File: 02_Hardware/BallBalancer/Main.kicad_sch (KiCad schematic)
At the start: 59 parts, among them J1 USB_B_Micro, J2 Raspberry PI UART, J3 SWD, J4 Reference switch 1, J5 ENCODER 1, J6 ENCODER 2, J7 Reference switch 2, U1 STM32L412K8Tx, U2 USBLC6-2SC6

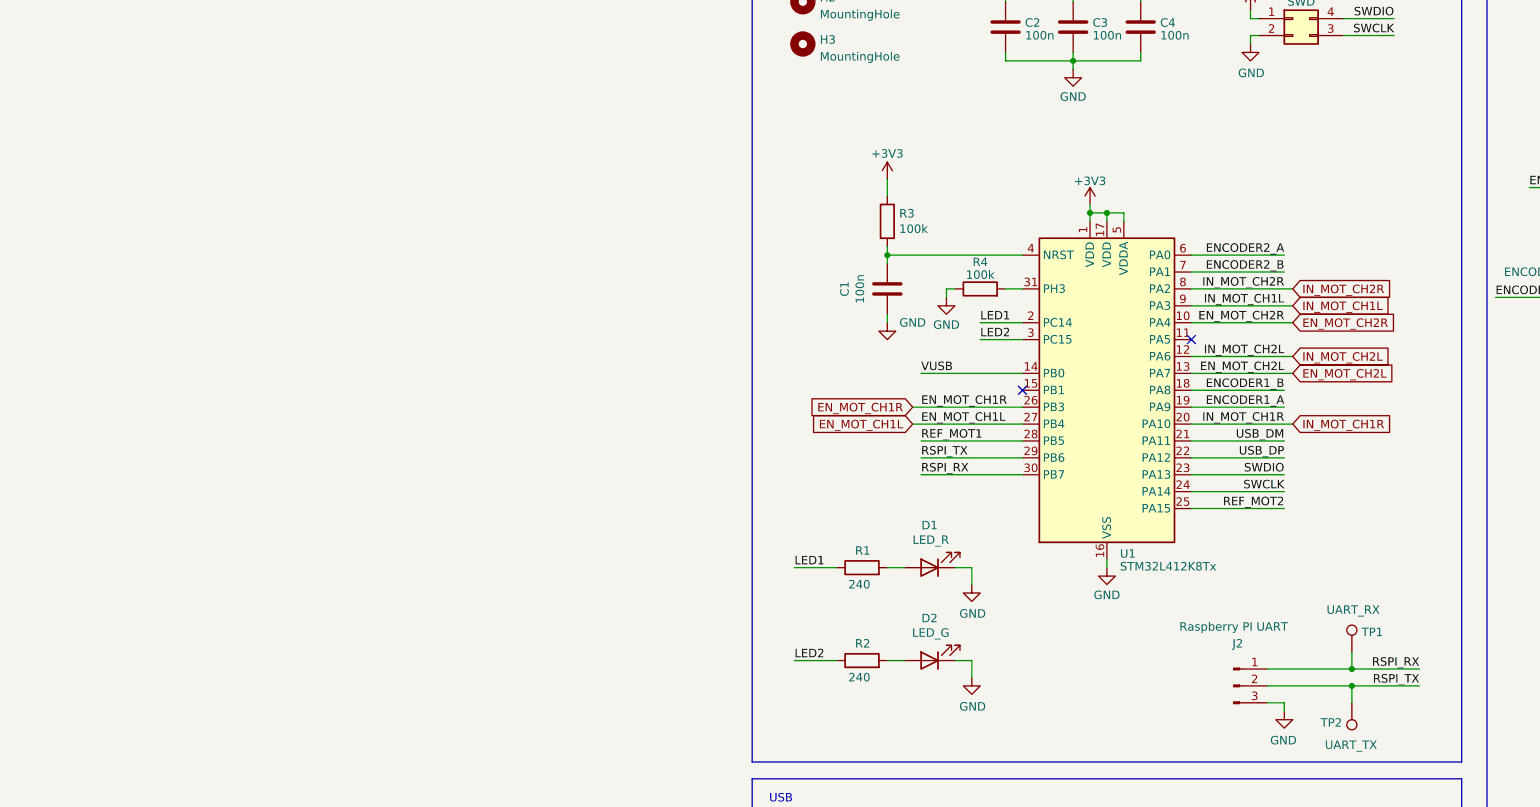
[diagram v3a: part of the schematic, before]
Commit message: replace microcontroller
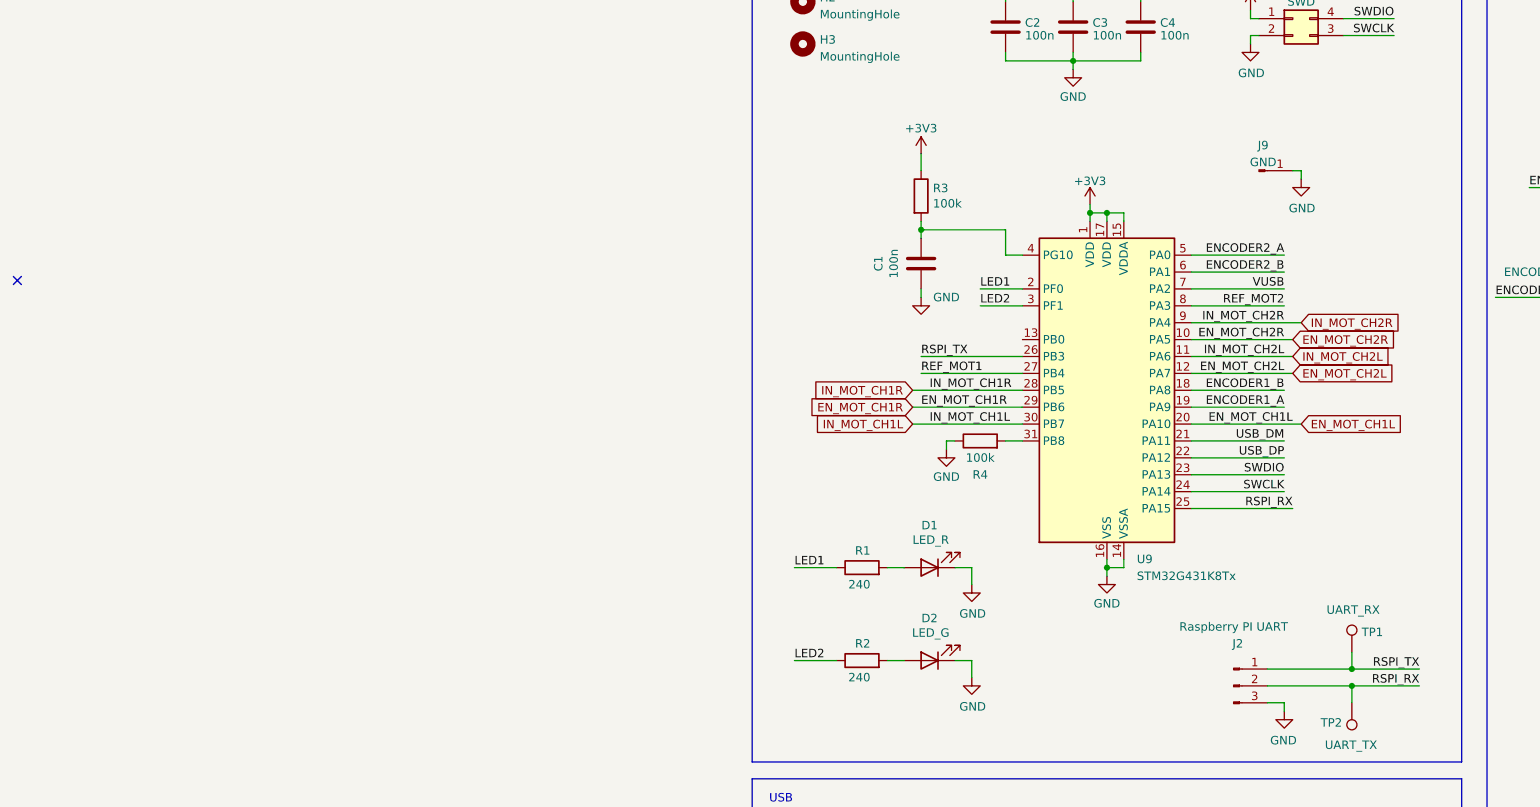
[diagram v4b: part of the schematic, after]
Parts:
- removed U1: STM32L412K8Tx, Package_QFP:LQFP-32_7x7mm_P0.8mm, symbol MCU_ST_STM32L4:STM32L412K8Tx
- added J9: GND, Connector_PinHeader_2.54mm:PinHeader_1x01_P2.54mm_Vertical, symbol Connector:Conn_01x01_Pin
- added U9: STM32G431K8Tx, Package_QFP:LQFP-32_7x7mm_P0.8mm, symbol MCU_ST_STM32G4:STM32G431K8Tx
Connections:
- net +3V3: now also U9.1 (VDD), U9.15 (VDDA), U9.17 (VDD)
- net ENCODER1_A: now also U9.19 (PA9)
- net ENCODER1_B: now also U9.18 (PA8)
- net ENCODER2_A: now also U9.5 (PA0)
- net ENCODER2_B: now also U9.6 (PA1)
- net EN_MOT_CH1L: now also U9.20 (PA10)
- net EN_MOT_CH1R: now also U9.29 (PB6)
- net EN_MOT_CH2L: now also U9.12 (PA7)
- net EN_MOT_CH2R: now also U9.10 (PA5)
- net GND: now also J9.1 (Pin_1), U9.14 (VSSA), U9.16 (VSS), U9.32 (VSS)
- net IN_MOT_CH1L: now also U9.30 (PB7)
- net IN_MOT_CH1R: now also U9.28 (PB5)
- net IN_MOT_CH2L: now also U9.11 (PA6)
- net IN_MOT_CH2R: now also U9.9 (PA4)
- net LED1: now also U9.2 (PF0)
- net LED2: now also U9.3 (PF1)
- net REF_MOT1: now also U9.27 (PB4)
- net REF_MOT2: now also U9.8 (PA3)
- net RSPI_RX: now also J2.2 (Pin_2), TP2.1, U9.25 (PA15); no longer J2.1 (Pin_1), TP1.1
- net RSPI_TX: now also J2.1 (Pin_1), TP1.1, U9.26 (PB3); no longer J2.2 (Pin_2), TP2.1
- net SWCLK: now also U9.24 (PA14)
- net SWDIO: now also U9.23 (PA13)
- net USB_DM: now also U9.21 (PA11)
- net USB_DP: now also U9.22 (PA12)
- net VUSB: now also U9.7 (PA2)
- net at R4.2: now also U9.31 (PB8)
- net at C1.2, R3.2: now also U9.4 (PG10)
- no-connect marks 5 -> 4
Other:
- moved on the sheet: C1, R3, R4

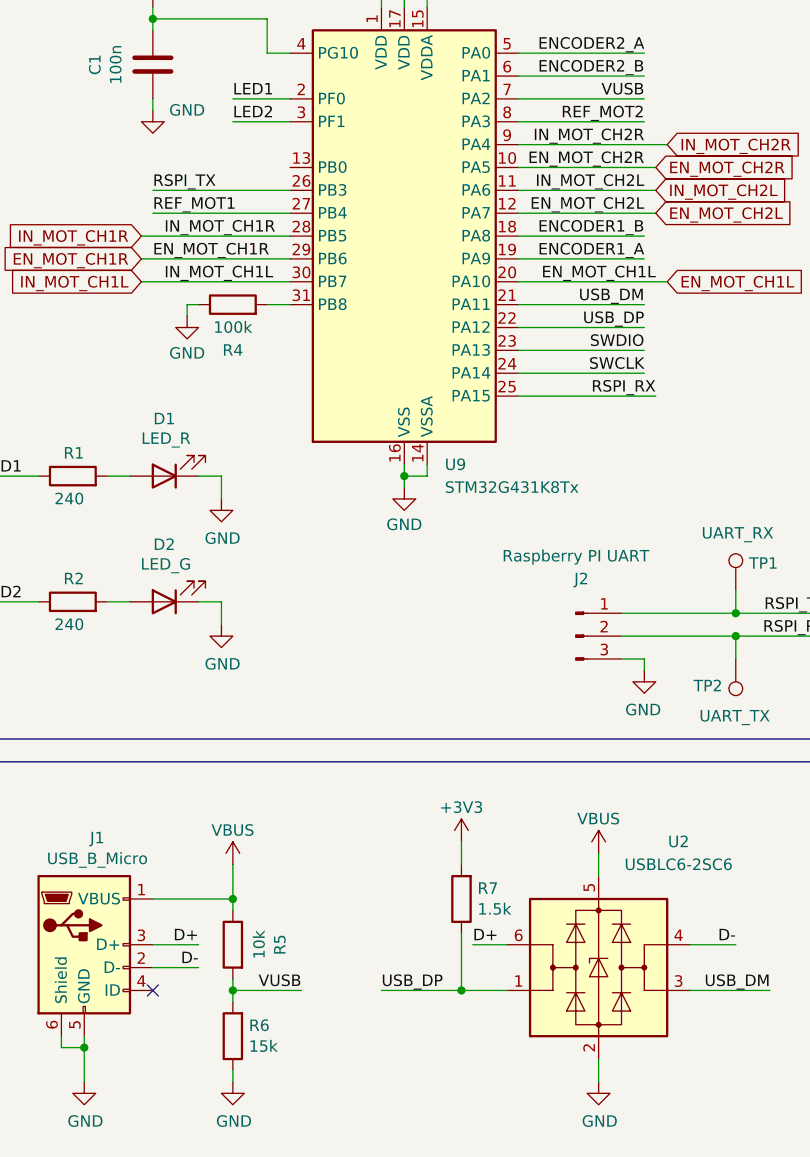
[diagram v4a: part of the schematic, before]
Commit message: Layout completed with stm32g431
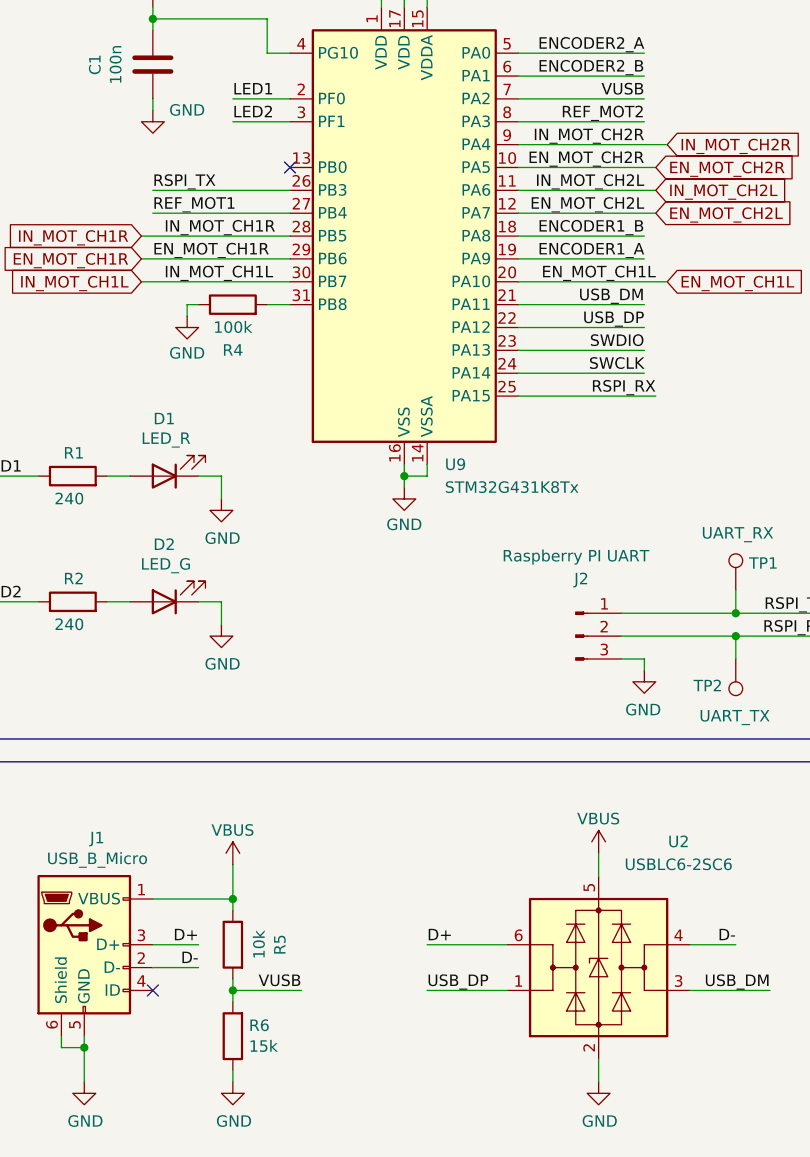
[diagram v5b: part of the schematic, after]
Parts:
- removed R7: 1.5k, Resistor_SMD:R_0603_1608Metric, symbol Device:R
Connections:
- no-connect marks 4 -> 5
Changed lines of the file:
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@@
   (junction (at 157.48 72.39) (diameter 0) (color 0 0 0 0)
   )
-  (junction (at 73.66 170.18) (diameter 0) (color 0 0 0 0)
-  )
   (junction (at 104.14 128.27) (diameter 0) (color 0 0 0 0)
   )
@@
   (junction (at 237.49 72.39) (diameter 0) (color 0 0 0 0)
   )
+  (no_connect (at 54.61 78.74))
   (no_connect (at 160.02 39.37))
   (no_connect (at 39.37 170.18))
@@
     (stroke (width 0) (type default))
   )
+  (wire (pts (xy 69.85 170.18) (xy 78.74 170.18))
+    (stroke (width 0) (type default))
+  )
   (wire (pts (xy 237.49 64.77) (xy 237.49 72.39))
     (stroke (width 0) (type default))
@@
     (stroke (width 0) (type default))
   )
-  (wire (pts (xy 78.74 170.18) (xy 73.66 170.18))
-    (stroke (width 0) (type default))
-  )
   (wire (pts (xy 237.49 72.39) (xy 237.49 74.93))
     (stroke (width 0) (type default))
@@
     (stroke (width 0) (type default))
   )
-  (wire (pts (xy 74.93 165.1) (xy 78.74 165.1))
+  (wire (pts (xy 69.85 165.1) (xy 78.74 165.1))
     (stroke (width 0) (type default))
   )
@@
     (stroke (width 0) (type default))
   )
-  (wire (pts (xy 73.66 163.83) (xy 73.66 170.18))
-    (stroke (width 0) (type default))
-  )
   (wire (pts (xy 91.44 133.35) (xy 93.98 133.35))
     (stroke (width 0) (type default))
@@
     (stroke (width 0) (type default))
   )
-  (wire (pts (xy 64.77 170.18) (xy 73.66 170.18))
-    (stroke (width 0) (type default))
-  )
   (wire (pts (xy 88.9 30.48) (xy 88.9 29.21))
     (stroke (width 0) (type default))
@@
     (stroke (width 0) (type default))
   )
-  (wire (pts (xy 73.66 153.67) (xy 73.66 156.21))
-    (stroke (width 0) (type default))
-  )
   (wire (pts (xy 93.98 101.6) (xy 80.01 101.6))
     (stroke (width 0) (type default))
@@
     (effects (font (size 1.27 1.27)) (justify left bottom))
   )
-  (label "D+" (at 74.93 165.1 0) (fields_autoplaced)
+  (label "D+" (at 69.85 165.1 0) (fields_autoplaced)
     (effects (font (size 1.27 1.27)) (justify left bottom))
   )
@@
     (effects (font (size 1.27 1.27)) (justify right bottom))
   )
-  (label "USB_DP" (at 64.77 170.18 0) (fields_autoplaced)
+  (label "USB_DP" (at 69.85 170.18 0) (fields_autoplaced)
     (effects (font (size 1.27 1.27)) (justify left bottom))
   )
@@
     )
   )
-  (symbol (lib_id "power:+3V3") (at 73.66 153.67 0) (unit 1)
-    (in_bom yes) (on_board yes) (dnp no) (fields_autoplaced)
-    (property "Reference" "#PWR013" (at 73.66 157.48 0)
-      (effects (font (size 1.27 1.27)) hide)
-    )
-    (property "Value" "+3V3" (at 73.66 149.86 0)
-      (effects (font (size 1.27 1.27)))
-    )
-    (property "Footprint" "" (at 73.66 153.67 0)
-      (effects (font (size 1.27 1.27)) hide)
-    )
-    (property "Datasheet" "" (at 73.66 153.67 0)
-      (effects (font (size 1.27 1.27)) hide)
-    )
-    (pin "1")
-    (instances
-      (project "BallBalancer"
-        (path "/d139795d-9e27-4394-be32-ac05c337c17d/97f62c80-ac17-4829-9f2c-b4ea071a8da4"
-          (reference "#PWR013") (unit 1)
-        )
-      )
-    )
-  )
   (symbol (lib_id "power:GND") (at 31.75 180.34 0) (unit 1)
     (in_bom yes) (on_board yes) (dnp no)
@@
         )
       )
-    )
-  )
-  (symbol (lib_id "Device:R") (at 73.66 160.02 180) (unit 1)
-    (in_bom yes) (on_board yes) (dnp no)
-    (property "Reference" "R7" (at 75.438 158.8516 0)
-      (effects (font (size 1.27 1.27)) (justify right))
-    )
-    (property "Value" "1.5k" (at 75.438 161.163 0)
-      (effects (font (size 1.27 1.27)) (justify right))
-    )
-    (property "Footprint" "Resistor_SMD:R_0603_1608Metric" (at 75.438 160.02 90)
-      (effects (font (size 1.27 1.27)) hide)
-    )
-    (property "Datasheet" "" (at 73.66 160.02 0)
-      (effects (font (size 1.27 1.27)) hide)
-    )
-    (property "Hersteller Nr." "CRCW06031K50JNEAC" (at 73.66 160.02 0)
-      (effects (font (size 1.27 1.27)) hide)
-    )
-    (property "Mouser Nr." "71-CRCW06031K50JNEAC" (at 73.66 160.02 0)
-      (effects (font (size 1.27 1.27)) hide)
-    )
-    (property "Info" "75V; 5%; 100mW; -55C; +155C" (at 73.66 160.02 0)
-      (effects (font (size 1.27 1.27)) hide)
-    )
-    (pin "1")
-    (pin "2")
-    (instances
-      (project "BallBalancer"
-        (path "/d139795d-9e27-4394-be32-ac05c337c17d/97f62c80-ac17-4829-9f2c-b4ea071a8da4"
-          (reference "R7") (unit 1)
-        )
-      )
-      (project "Spanner"
-        (path "/ed8d0ee4-83e3-4807-8850-ea20e8975bf5/cb73e00e-b752-4474-a136-20146bf8e401"
-          (reference "R6") (unit 1)
-        )
-      )

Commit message: update layout
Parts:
- removed J9: GND, Connector_PinHeader_2.54mm:PinHeader_1x01_P2.54mm_Vertical, symbol Connector:Conn_01x01_Pin
- added J10: GND, Connector_PinHeader_2.54mm:PinHeader_1x02_P2.54mm_Vertical, symbol Connector:Conn_01x02_Pin
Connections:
- net GND: now also J10.1 (Pin_1), J10.2 (Pin_2)
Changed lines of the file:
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@@
   (junction (at 229.87 72.39) (diameter 0) (color 0 0 0 0)
+  )
+  (junction (at 86.36 53.34) (diameter 0) (color 0 0 0 0)
   )
   (junction (at 166.37 128.27) (diameter 0) (color 0 0 0 0)
@@
     (stroke (width 0) (type default))
   )
-  (wire (pts (xy 95.25 53.34) (xy 96.52 53.34))
+  (wire (pts (xy 85.09 53.34) (xy 86.36 53.34))
     (stroke (width 0) (type default))
   )
@@
     (stroke (width 0) (type default))
   )
-  (wire (pts (xy 96.52 53.34) (xy 96.52 54.61))
+  (wire (pts (xy 86.36 53.34) (xy 86.36 54.61))
     (stroke (width 0) (type default))
   )
@@
     (stroke (width 0) (type default))
   )
-  (wire (pts (xy 104.14 165.1) (xy 99.06 165.1))
+  (wire (pts (xy 99.06 165.1) (xy 107.95 165.1))
     (stroke (width 0) (type default))
   )
@@
     (stroke (width 0) (type default))
   )
+  (wire (pts (xy 86.36 50.8) (xy 86.36 53.34))
+    (stroke (width 0) (type default))
+  )
   (wire (pts (xy 160.02 36.83) (xy 177.8 36.83))
     (stroke (width 0) (type default))
@@
   )
   (wire (pts (xy 179.07 128.27) (xy 190.5 128.27))
+    (stroke (width 0) (type default))
+  )
+  (wire (pts (xy 85.09 50.8) (xy 86.36 50.8))
     (stroke (width 0) (type default))
   )
@@
     (effects (font (size 1.27 1.27)) (justify left bottom))
   )
-  (label "D-" (at 104.14 165.1 180) (fields_autoplaced)
+  (label "D-" (at 107.95 165.1 180) (fields_autoplaced)
     (effects (font (size 1.27 1.27)) (justify right bottom))
   )
@@
     )
   )
-  (symbol (lib_id "power:GND") (at 96.52 54.61 0) (unit 1)
-    (in_bom yes) (on_board yes) (dnp no)
-    (property "Reference" "#PWR090" (at 96.52 60.96 0)
-      (effects (font (size 1.27 1.27)) hide)
-    )
-    (property "Value" "GND" (at 96.647 59.0042 0)
-      (effects (font (size 1.27 1.27)))
-    )
-    (property "Footprint" "" (at 96.52 54.61 0)
-      (effects (font (size 1.27 1.27)) hide)
-    )
-    (property "Datasheet" "" (at 96.52 54.61 0)
+  (symbol (lib_id "power:GND") (at 86.36 54.61 0) (unit 1)
+    (in_bom yes) (on_board yes) (dnp no)
+    (property "Reference" "#PWR090" (at 86.36 60.96 0)
+      (effects (font (size 1.27 1.27)) hide)
+    )
+    (property "Value" "GND" (at 86.487 59.0042 0)
+      (effects (font (size 1.27 1.27)))
+    )
+    (property "Footprint" "" (at 86.36 54.61 0)
+      (effects (font (size 1.27 1.27)) hide)
+    )
+    (property "Datasheet" "" (at 86.36 54.61 0)
       (effects (font (size 1.27 1.27)) hide)
     )
@@
     )
   )
+  (symbol (lib_id "Connector:Conn_01x02_Pin") (at 80.01 50.8 0) (unit 1)
+    (in_bom yes) (on_board yes) (dnp no) (fields_autoplaced)
+    (property "Reference" "J10" (at 80.645 46.99 0)
+      (effects (font (size 1.27 1.27)))
+    )
+    (property "Value" "GND" (at 80.645 49.53 0)
+      (effects (font (size 1.27 1.27)))
+    )
+    (property "Footprint" "Connector_PinHeader_2.54mm:PinHeader_1x02_P2.54mm_Vertical" (at 80.01 50.8 0)
+      (effects (font (size 1.27 1.27)) hide)
+    )
+    (property "Datasheet" "~" (at 80.01 50.8 0)
+      (effects (font (size 1.27 1.27)) hide)
+    )
+    (pin "1")
+    (pin "2")
+    (instances
+      (project "BallBalancer"
+        (path "/d139795d-9e27-4394-be32-ac05c337c17d/97f62c80-ac17-4829-9f2c-b4ea071a8da4"
+          (reference "J10") (unit 1)
+        )
+      )
+    )
+  )
   (symbol (lib_id "Device:R") (at 30.48 127 90) (unit 1)
     (in_bom yes) (on_board yes) (dnp no)
@@
         )
       )
-    )
-  )
-  (symbol (lib_id "Connector:Conn_01x01_Pin") (at 90.17 53.34 0) (unit 1)
-    (in_bom yes) (on_board yes) (dnp no) (fields_autoplaced)
-    (property "Reference" "J9" (at 90.805 49.53 0)
-      (effects (font (size 1.27 1.27)))
-    )
-    (property "Value" "GND" (at 90.805 52.07 0)
-      (effects (font (size 1.27 1.27)))
-    )
-    (property "Footprint" "Connector_PinHeader_2.54mm:PinHeader_1x01_P2.54mm_Vertical" (at 90.17 53.34 0)
-      (effects (font (size 1.27 1.27)) hide)
-    )
-    (property "Datasheet" "~" (at 90.17 53.34 0)
-      (effects (font (size 1.27 1.27)) hide)
-    )
-    (pin "1")
-    (instances
-      (project "BallBalancer"
-        (path "/d139795d-9e27-4394-be32-ac05c337c17d/97f62c80-ac17-4829-9f2c-b4ea071a8da4"
-          (reference "J9") (unit 1)
-        )
-      )
